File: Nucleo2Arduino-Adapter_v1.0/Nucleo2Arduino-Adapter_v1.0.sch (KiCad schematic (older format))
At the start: 12 parts, among them J1 TI_BOOSTER_40_J1, J2 TI_BOOSTER_40_J2, J3 TI_BOOSTER_40_J3, J4 TI_BOOSTER_40_J4, P1 Power, P2 Analog, P3 Digital, P4 Digital, P5 CONN_1, P6 CONN_1, P7 CONN_1, P8 CONN_1

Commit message: fixed Arduino pin symbol
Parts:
- added U?: ARDUINO_ICSP, symbol ARDUINO_ICSP
- P1: symbol CONN_8 -> ARDUINO_POWER
- P2: symbol CONN_6 -> ARDUINO_ANALOG
- P3: symbol CONN_10 -> ARDUINO_IOH
- P4: symbol CONN_8 -> ARDUINO_IOL
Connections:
- net labels removed: +3.3V, 0(Rx), 1(Tx), 10(**/SS), 11(**/MOSI), 12(MISO), 13(SCK), 2, 3(**), 4, 5(**), 6(**), 7, 8, 9(**), A0, A1, A2, A3, A4(SDA), A5(SCL), AREF, IOREF, Reset, Vin
- wire segments 38 -> 0
- no-connect marks 5 -> 4
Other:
- note removed: "Shield for Arduino that uses\nthe same pin disposition\nlike "Uno" board Rev 3."
- moved on the sheet: P5, P6, P7, P8

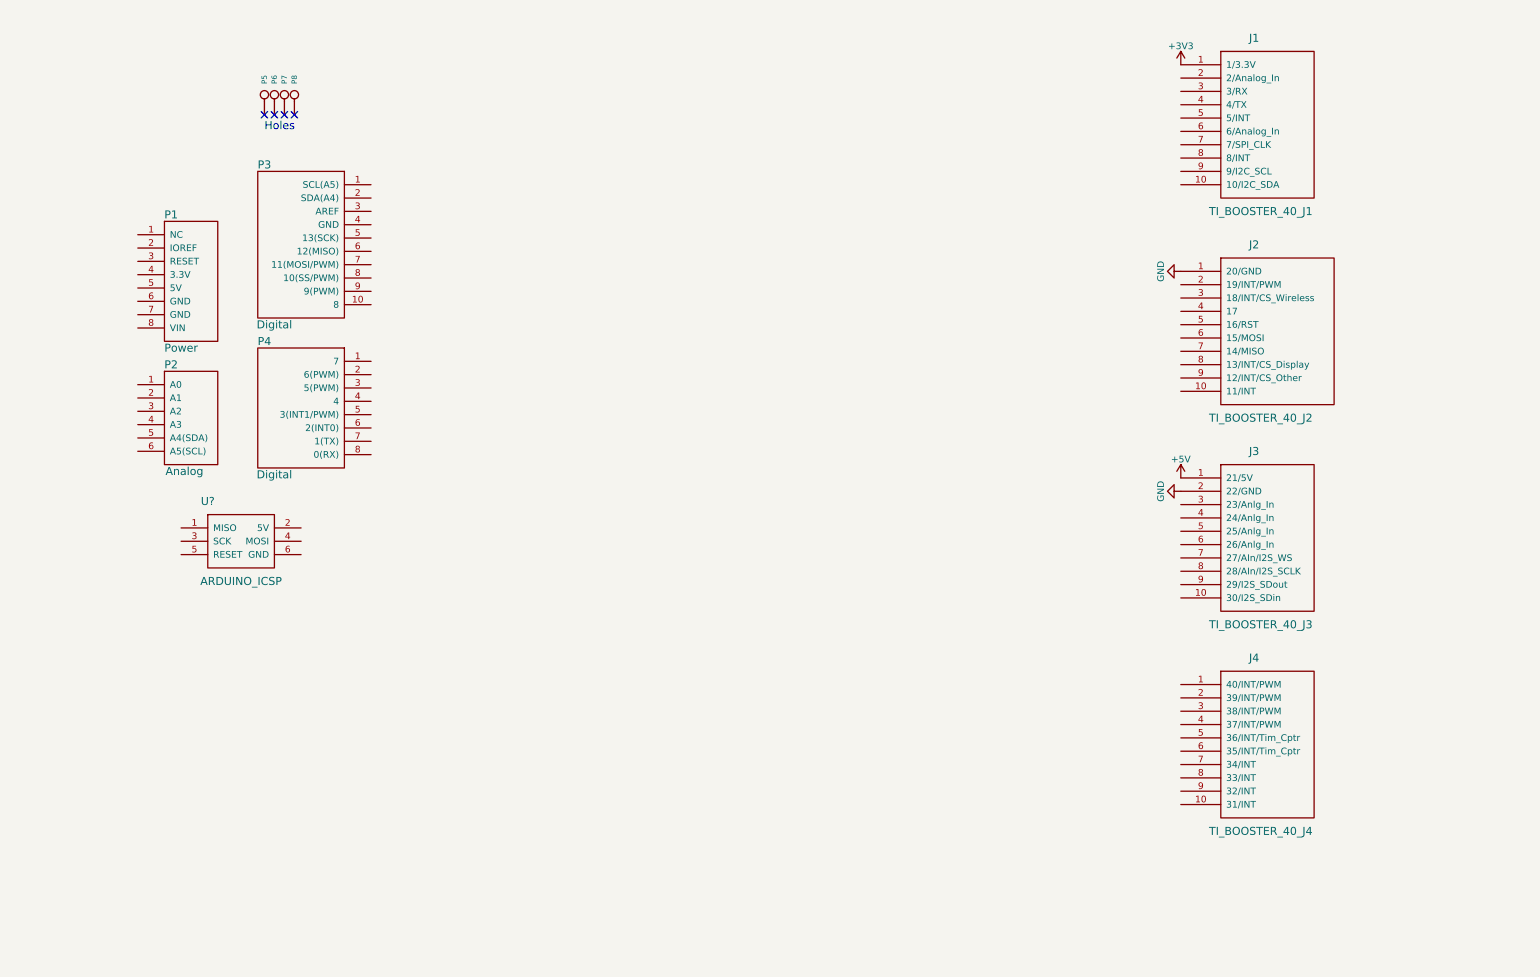
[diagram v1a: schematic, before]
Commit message: Added ICSP header, Fixed Ardino/BSTPCK Symbols, Added connection
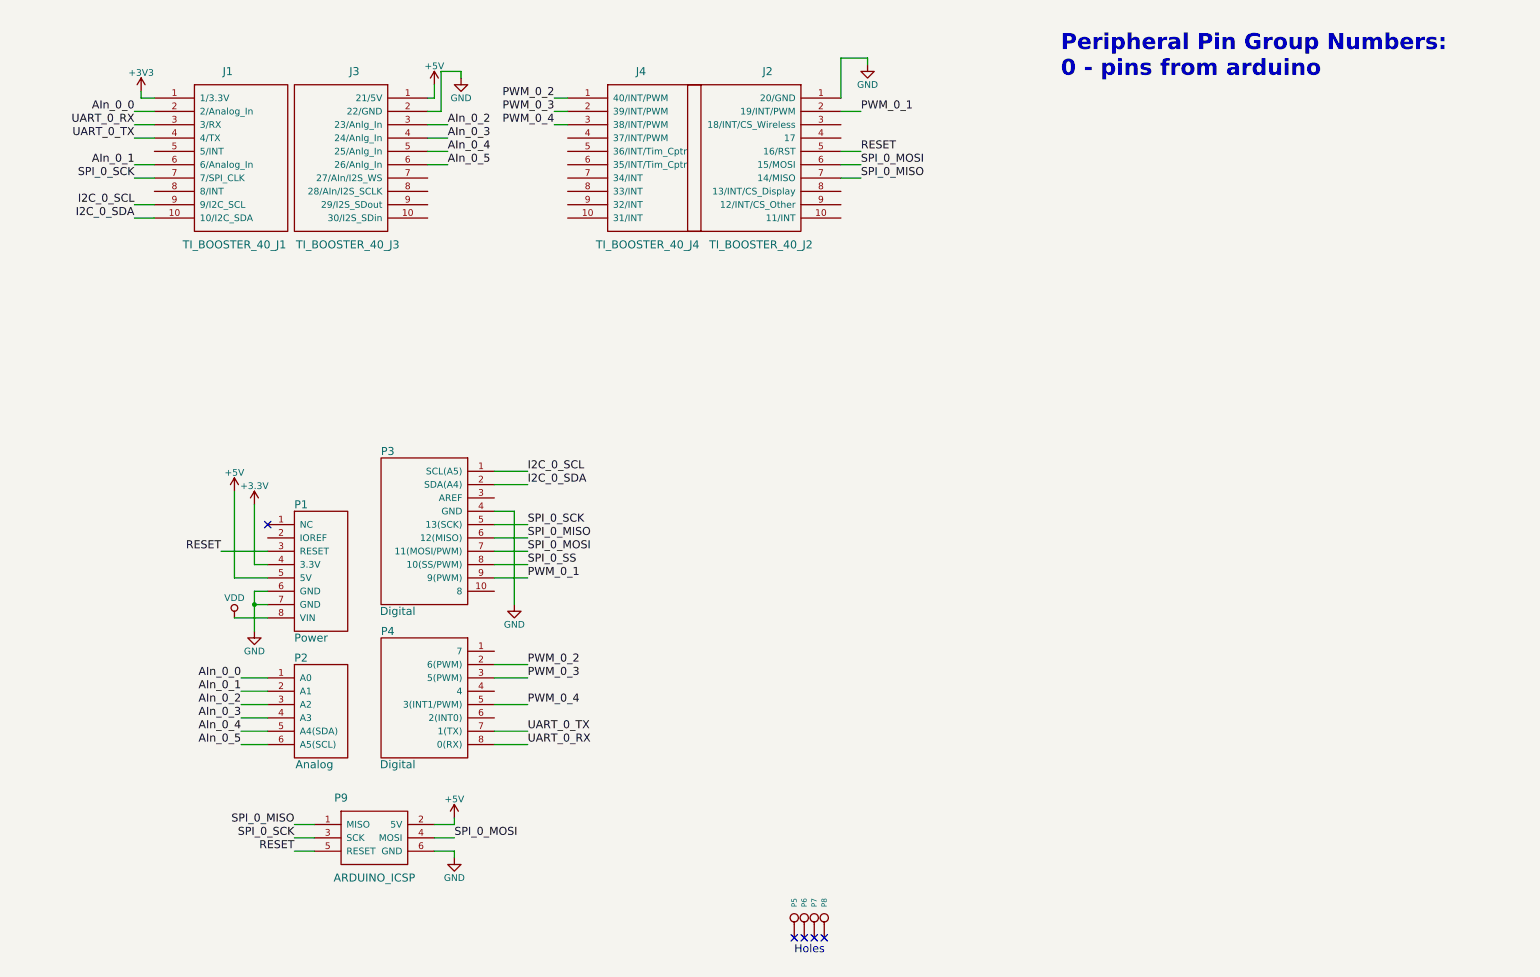
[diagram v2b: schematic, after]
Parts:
- P9: renamed from U?; footprint (none) -> Pin_Headers:Pin_Header_Straight_2x03
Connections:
- net +3V3: now also P1.4 (3.3V)
- net +5V: now also P1.5 (5V), P9.2 (5V)
- net GND: now also P1.6 (GND), P1.7 (GND), P3.4 (GND), P9.6 (GND)
- net RESET: now reaches P1.3 (RESET)
- net RESET: now also J2.5 (16/RST), P9.5 (RESET)
- net VDD: now reaches P1.8 (VIN)
- net AIn_0_0: now reaches P2.1 (A0)
- net AIn_0_0: now also J1.2 (2/Analog_In)
- net AIn_0_1: now reaches P2.2 (A1)
- net AIn_0_1: now also J1.6 (6/Analog_In)
- net AIn_0_2: now reaches P2.3 (A2)
- net AIn_0_2: now also J3.3 (23/Anlg_In)
- net AIn_0_3: now reaches P2.4 (A3)
- net AIn_0_3: now also J3.4 (24/Anlg_In)
- net AIn_0_4: now reaches P2.5 (A4(SDA))
- net AIn_0_4: now also J3.5 (25/Anlg_In)
- net AIn_0_5: now reaches P2.6 (A5(SCL))
- net AIn_0_5: now also J3.6 (26/Anlg_In)
- net PWM_0_2: now reaches P4.2 (6(PWM))
- net PWM_0_2: now also J4.1 (40/INT/PWM)
- net PWM_0_3: now reaches P4.3 (5(PWM))
- net PWM_0_3: now also J4.2 (39/INT/PWM)
- net PWM_0_4: now reaches P4.5 (3(INT1/PWM))
- net PWM_0_4: now also J4.3 (38/INT/PWM)
- net UART_0_TX: now reaches P4.7 (1(TX))
- net UART_0_TX: now also J1.4 (4/TX)
- net UART_0_RX: now reaches P4.8 (0(RX))
- net UART_0_RX: now also J1.3 (3/RX)
- net I2C_0_SCL: now reaches P3.1 (SCL(A5))
- net I2C_0_SCL: now also J1.9 (9/I2C_SCL)
- net I2C_0_SDA: now reaches P3.2 (SDA(A4))
- net I2C_0_SDA: now also J1.10 (10/I2C_SDA)
- net SPI_0_SCK: now reaches P3.5 (13(SCK))
- net SPI_0_SCK: now also J1.7 (7/SPI_CLK), P9.3 (SCK)
- net SPI_0_MISO: now reaches P3.6 (12(MISO))
- net SPI_0_MISO: now also J2.7 (14/MISO), P9.1 (MISO)
- net SPI_0_MOSI: now reaches P3.7 (11(MOSI/PWM))
- net SPI_0_MOSI: now also J2.6 (15/MOSI), P9.4 (MOSI)
- net SPI_0_SS: now reaches P3.8 (10(SS/PWM))
- net PWM_0_1: now reaches P3.9 (9(PWM))
- net PWM_0_1: now also J2.2 (19/INT/PWM)
- no-connect marks 4 -> 5
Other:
- note added: "Peripheral Pin Group Numbers:\n0 - pins from arduino"
- moved on the sheet: J1, J2, J3, J4, P1, P2, P3, P4, P5, P6, P7, P8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

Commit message: added Nucleo Zio and Atmel XPro Header symbol
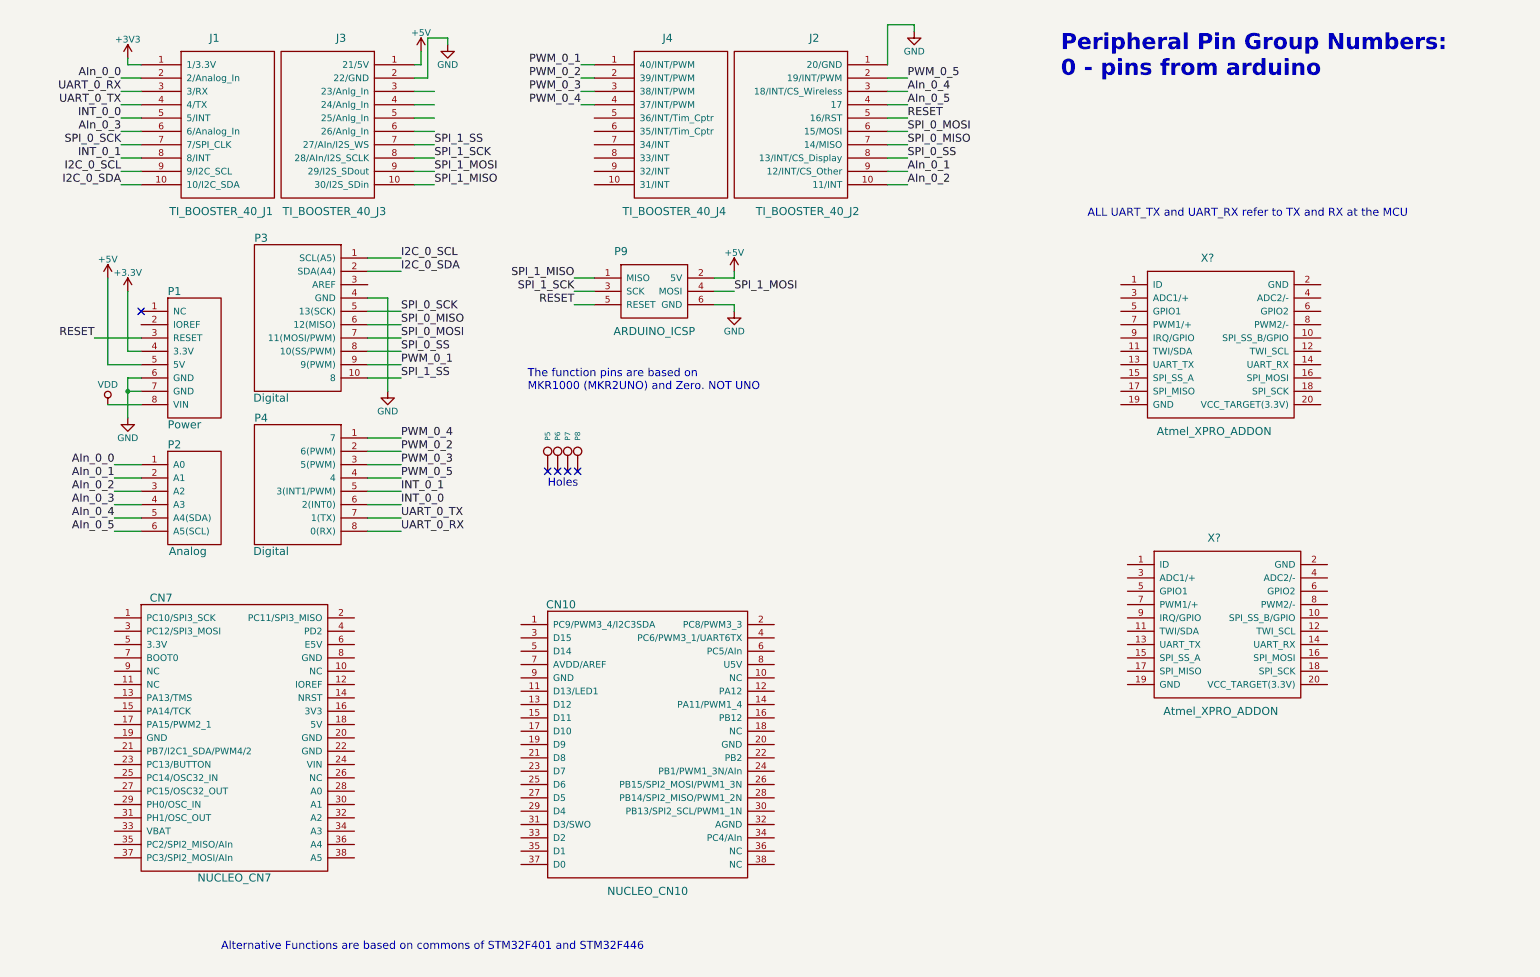
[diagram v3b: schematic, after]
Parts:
- added CN10: NUCLEO_CN10, symbol NUCLEO_CN10
- added CN7: NUCLEO_CN7, symbol NUCLEO_CN7
- added X? (x2): Atmel_XPRO_ADDON, symbol Atmel_XPRO_ADDON
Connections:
- net labels added: INT_0_0, INT_0_1, PWM_0_5, SPI_1_MISO, SPI_1_MOSI, SPI_1_SCK, SPI_1_SS
- wire segments 66 -> 82
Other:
- note added: "ALL UART_TX and UART_RX refer to TX and RX at the MCU"
- note added: "Alternative Functions are based on commons of STM32F401 and STM32F446"
- note added: "The function pins are based on\nMKR1000 (MKR2UNO) and Zero. NOT UNO"
- moved on the sheet: J1, J2, J3, J4, P1, P2, P3, P4, P5, P6, P7, P8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

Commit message: First draft of connection. Completed PCB pin position
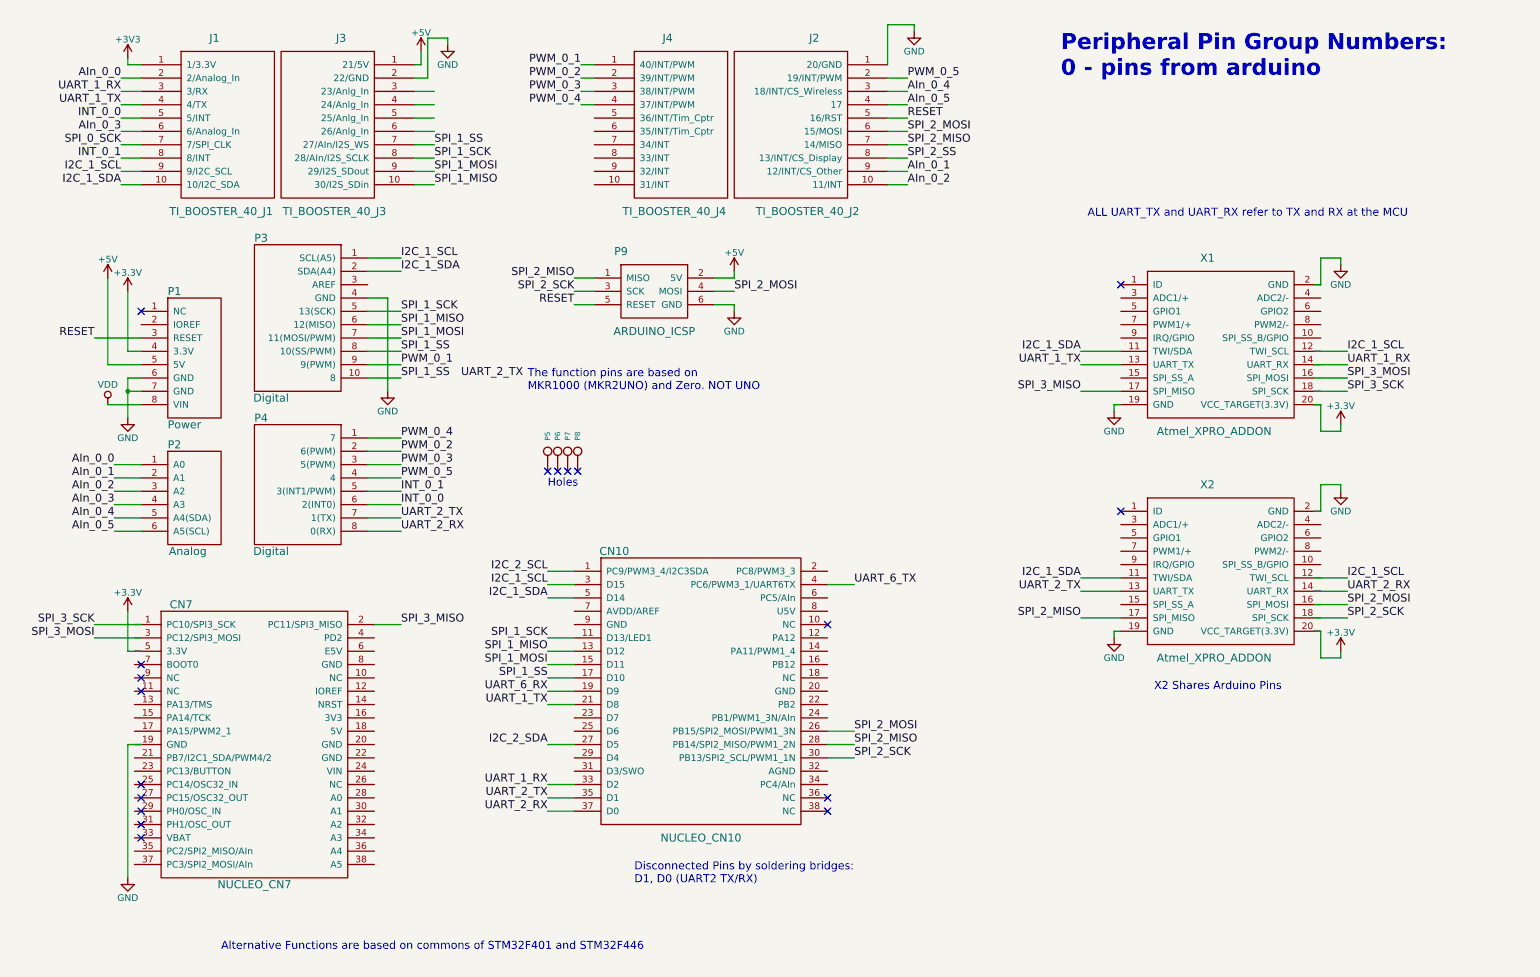
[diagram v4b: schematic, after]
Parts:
- CN10, CN7: footprint (none) -> Pin_Headers:Pin_Header_Straight_2x19
- X1, X2: renamed from X?; footprint (none) -> Pin_Headers:Pin_Header_Angled_2x10
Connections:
- net labels added: I2C_1_SCL, I2C_1_SDA, I2C_2_SCL, I2C_2_SDA, SPI_2_MISO, SPI_2_MOSI, SPI_2_SCK, SPI_2_SS, SPI_3_MISO, SPI_3_MOSI, SPI_3_SCK, UART_1_RX, UART_1_TX, UART_2_RX, UART_2_TX, UART_6_RX, UART_6_TX
- net labels removed: I2C_0_SCL, I2C_0_SDA, SPI_0_MISO, SPI_0_MOSI, SPI_0_SS, UART_0_RX, UART_0_TX
- wire segments 82 -> 140
- no-connect marks 5 -> 18
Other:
- note added: "Disconnected Pins by soldering bridges:\nD1, D0 (UART2 TX/RX)"
- note added: "X2 Shares Arduino Pins"
- moved on the sheet: CN10, CN7, X2

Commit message: Connections and PCB footprint completed. Needs routing
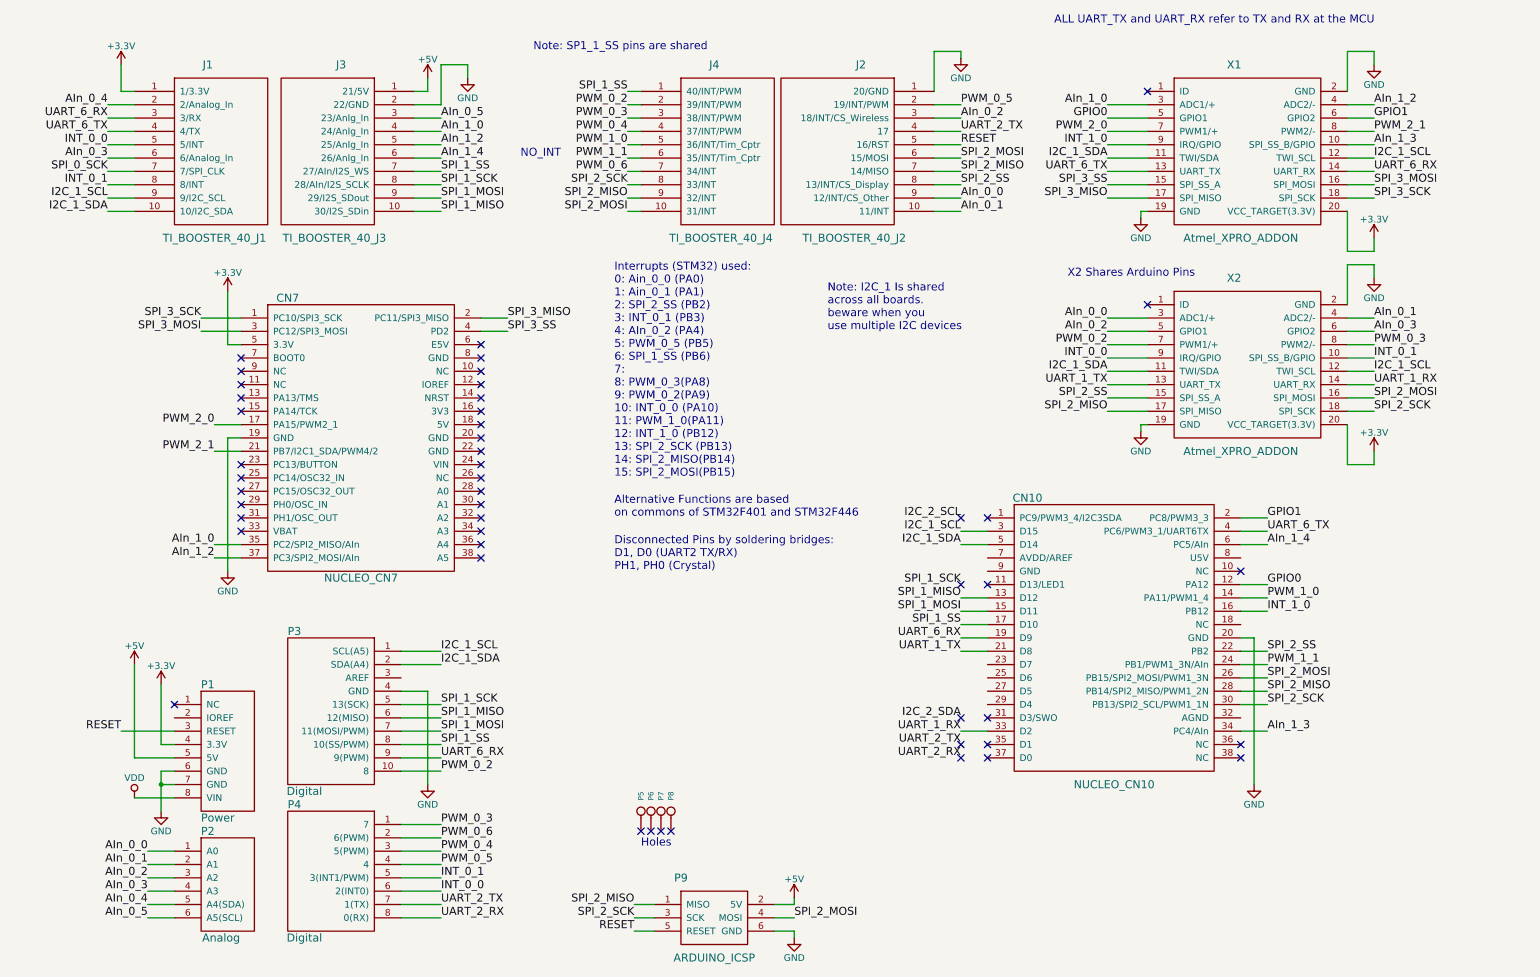
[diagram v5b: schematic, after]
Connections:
- net labels added: AIn_1_0, AIn_1_2, AIn_1_3, AIn_1_4, GPIO0, GPIO1, INT_1_0, PWM_0_6, PWM_1_0, PWM_1_1, PWM_2_0, PWM_2_1, SPI_3_SS
- net labels removed: +3V3, PWM_0_1
- wire segments 140 -> 170
- no-connect marks 18 -> 48
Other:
- note added: "Alternative Functions are based\non commons of STM32F401 and STM32F446"
- note added: "Disconnected Pins by soldering bridges:\nD1, D0 (UART2 TX/RX)\nPH1, PH0 (Crystal)"
- note added: "Interrupts (STM32) used:\n0: Ain_0_0 (PA0)\n1: Ain_0_1 (PA1)\n2: SPI_2_SS (PB2)\n3: INT_0_1 (PB3)\n4: AIn_0_2 (PA4)\n5: PWM_0_5 (PB5)\n6: SPI_1_SS (PB6)\n7: \n8: PWM_0_3(PA8)\n9: PWM_0_2(PA9)\n10: INT_0_0 (PA10)\n11: PWM_1_0(PA11)\n12: INT_1_0 (PB12)\n13: SPI_2_SCK (PB13)\n14: SPI_2_MISO(PB14)\n15: SPI_2_MOSI(PB15)"
- note added: "NO_INT"
- note added: "Note: I2C_1 Is shared\nacross all boards.\nbeware when you \nuse multiple I2C devices"
- note added: "Note: SP1_1_SS pins are shared"
- note removed: "Alternative Functions are based on commons of STM32F401 and STM32F446"
- note removed: "Disconnected Pins by soldering bridges:\nD1, D0 (UART2 TX/RX)"
- note removed: "Peripheral Pin Group Numbers:\n0 - pins from arduino"
- note removed: "The function pins are based on\nMKR1000 (MKR2UNO) and Zero. NOT UNO"
- moved on the sheet: CN10, CN7, J1, J2, J3, J4, P1, P2, P3, P4, P5, P6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
